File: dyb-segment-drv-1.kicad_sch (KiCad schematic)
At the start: 8 parts, among them U1 AP2112K-1.8, U2 SN74AUP2G08, U3 74AUC2G32, U4 Inverter_Schmitt_Dual

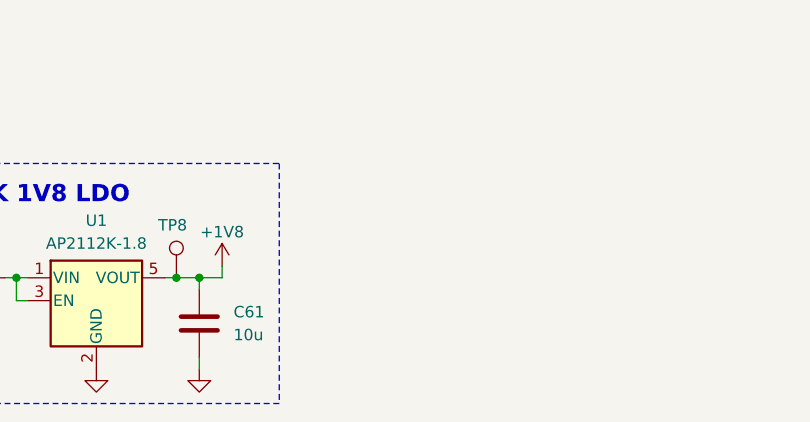
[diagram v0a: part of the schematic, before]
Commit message: schem: add cr2032 holder
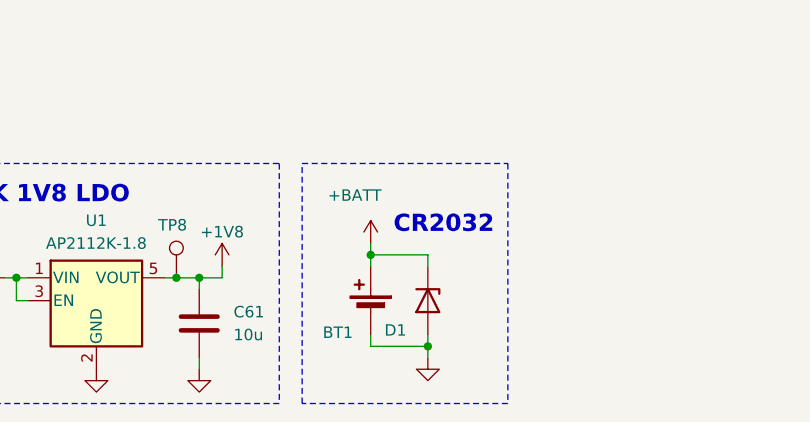
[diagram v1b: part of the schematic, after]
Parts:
- added BT1: Battery_Cell, GLCS:BatteryHolder_MYOUNG_BS-08-B2AA016, symbol Device:Battery_Cell
- added D1: H5VU10U, GLCS:Diode_DFN1006, symbol GLCS:H5VU10U
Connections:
- net +BATT: now also BT1.1 (+), D1.1 (K)
- net GND: now also BT1.2 (-), D1.2 (A)
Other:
- note added: "CR2032"

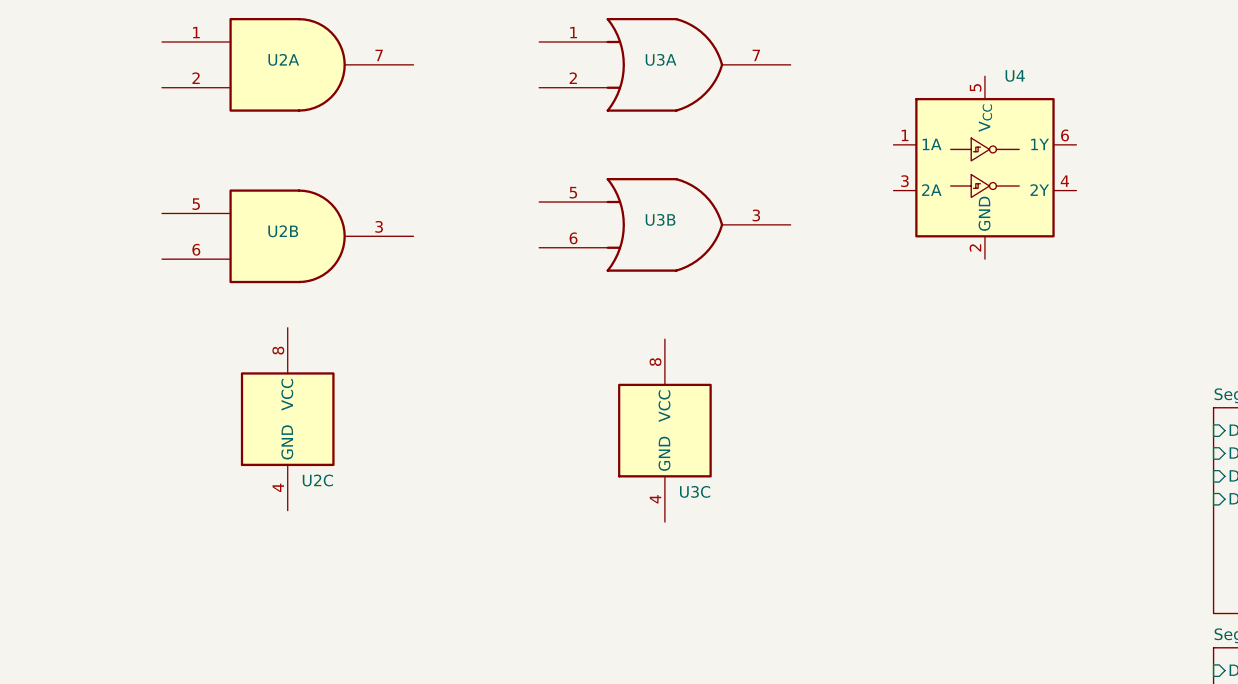
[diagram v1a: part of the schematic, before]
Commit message: schem: remove extra gates
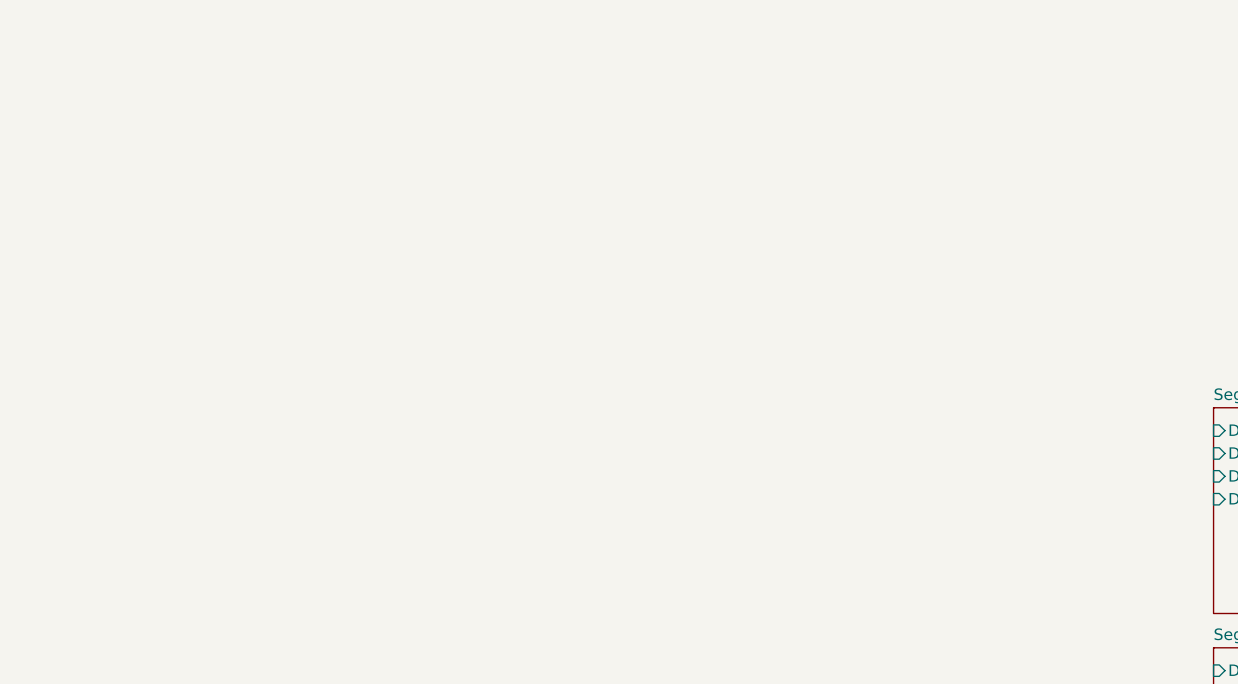
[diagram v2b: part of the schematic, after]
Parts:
- removed U2: SN74AUP2G08, Package_SO:VSSOP-8_2.3x2mm_P0.5mm, symbol GLCS:SN74AUP2G08
- removed U3: 74AUC2G32, Package_DFN_QFN:QFN-20-1EP_5x5mm_P0.65mm_EP3.35x3.35mm, symbol 74xGxx:74AUC2G32
- removed U4: Inverter_Schmitt_Dual, Package_TO_SOT_SMD:SOT-23-6, symbol 74xGxx:Inverter_Schmitt_Dual

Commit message: schem: add b2b connector
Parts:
- added J1: Conn_01x10, symbol Connector_Generic:Conn_01x10
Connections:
- net GND: now also J1.10 (Pin_10)
- new net A0: J1.1 (Pin_1)
- new net A1: J1.2 (Pin_2)
- new net A2: J1.3 (Pin_3)
- new net A3: J1.4 (Pin_4)
- new net B0: J1.5 (Pin_5)
- new net B1: J1.6 (Pin_6)
- new net B2: J1.7 (Pin_7)
- new net B3: J1.8 (Pin_8)
- no-connect marks 0 -> 1

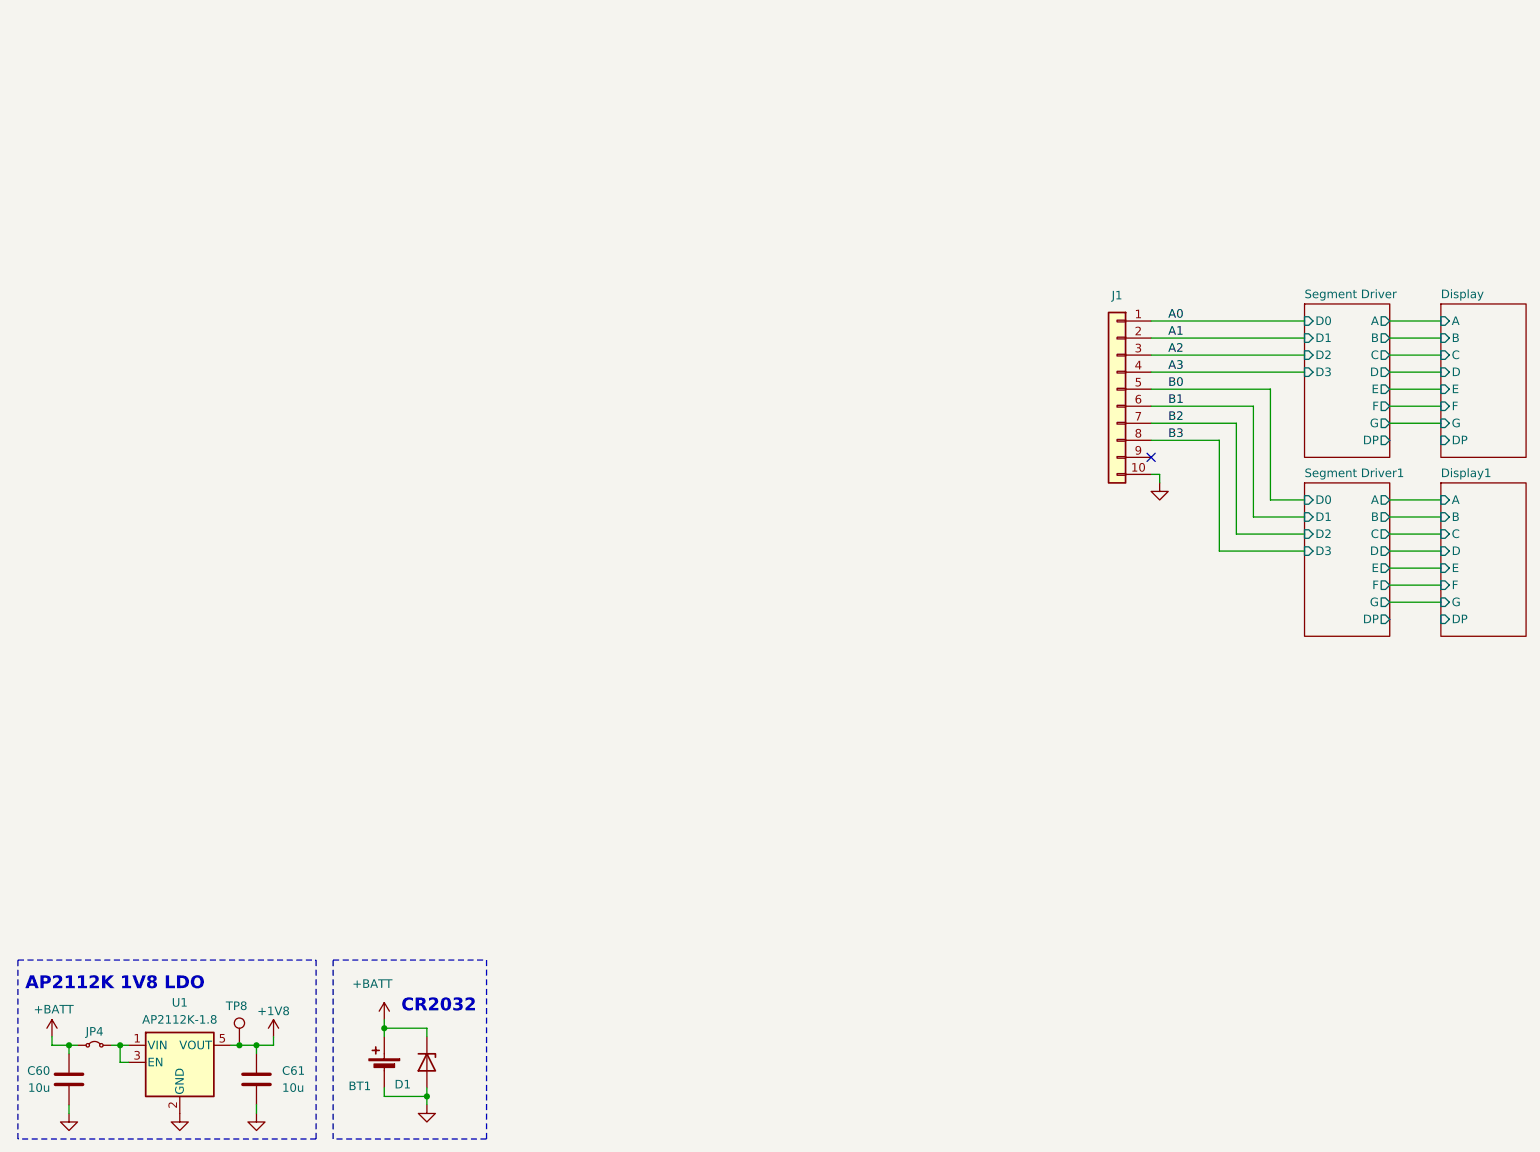
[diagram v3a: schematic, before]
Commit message: schem: add batt switch
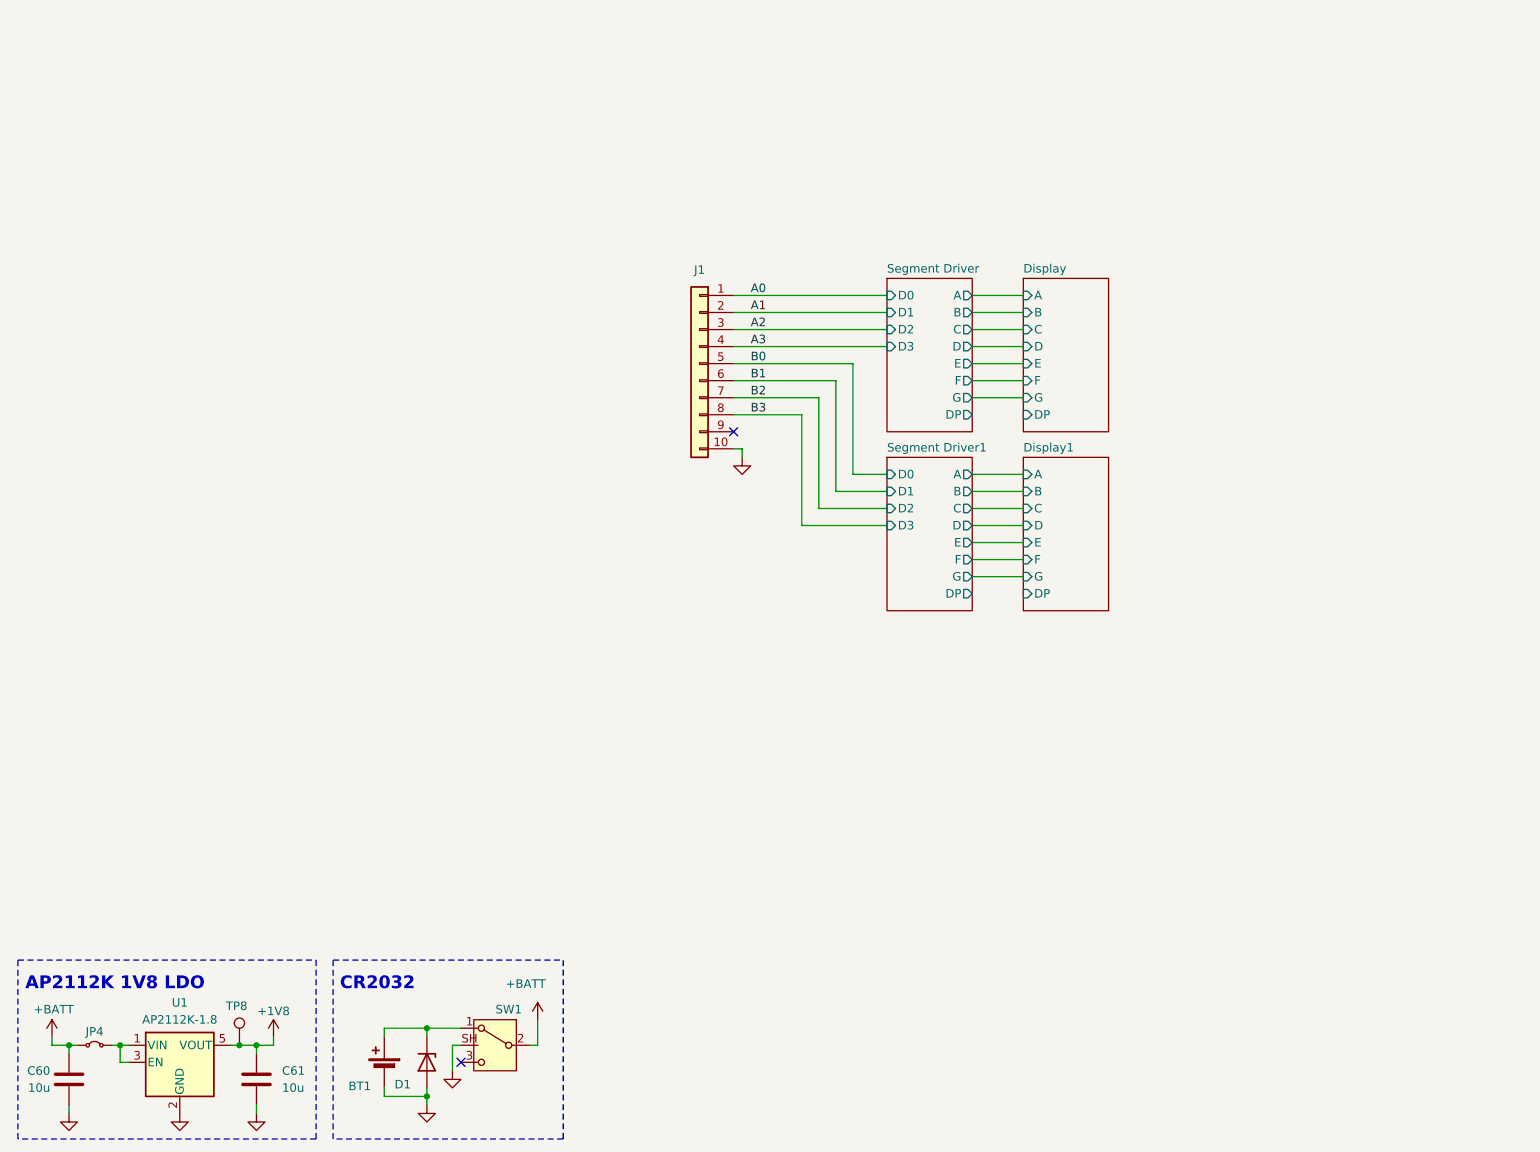
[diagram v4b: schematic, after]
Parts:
- added SW1: SW_SPDT, Button_Switch_SMD:SW_SPDT_Shouhan_MSK12C02, symbol Switch:SW_SPDT
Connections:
- net +BATT: now also SW1.2 (B); no longer BT1.1 (+), D1.1 (K)
- net GND: now also SW1.SH
- new net: BT1.1 (+), D1.1 (K), SW1.1 (A)
- no-connect marks 1 -> 2
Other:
- moved on the sheet: J1

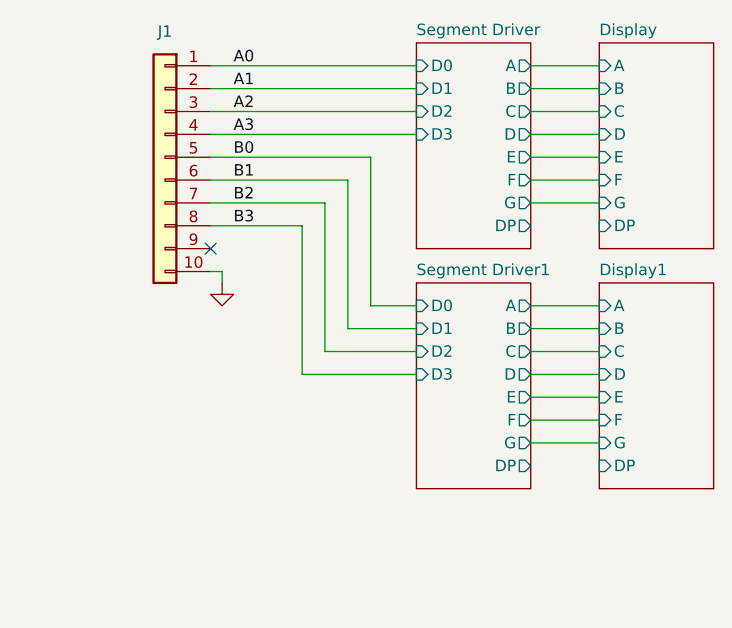
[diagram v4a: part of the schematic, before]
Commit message: schem: add test points
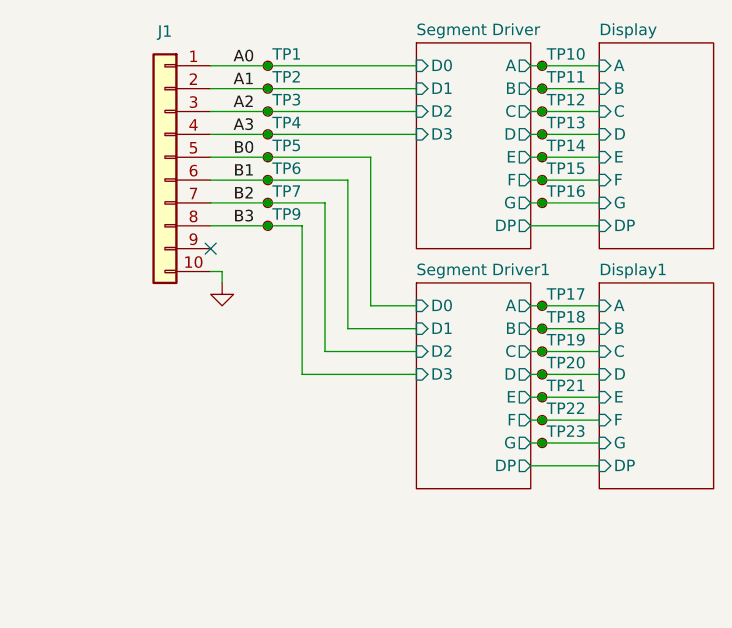
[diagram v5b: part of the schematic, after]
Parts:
- added TP1, TP10, TP11, TP12, TP13, TP14, TP15, TP16, TP17, TP18, TP19, TP2, TP20, TP21, TP22, TP23, TP3, TP4, TP5, TP6, TP7, TP9: TestPoint_Small, symbol Connector:TestPoint_Small
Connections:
- net A0: now also TP1.1
- net A1: now also TP2.1
- net A2: now also TP3.1
- net A3: now also TP4.1
- net B0: now also TP5.1
- net B1: now also TP6.1
- net B2: now also TP7.1
- net B3: now also TP9.1
- net Display/A: now also TP10.1
- net Display/B: now also TP11.1
- net Display/C: now also TP12.1
- net Display/D: now also TP13.1
- net Display/E: now also TP14.1
- net Display/F: now also TP15.1
- net Display/G: now also TP16.1
- net Display1/A: now also TP17.1
- net Display1/B: now also TP18.1
- net Display1/C: now also TP19.1
- net Display1/D: now also TP20.1
- net Display1/E: now also TP21.1
- net Display1/F: now also TP22.1
- net Display1/G: now also TP23.1

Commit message: schem: run and fix ERC
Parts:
- added TP26, TP27: TestPoint_Small, symbol Connector:TestPoint_Small
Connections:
- net Display/DP: now also TP27.1
- net Display1/DP: now also TP26.1
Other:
- sheet Segment Driver ports: added none; removed DP
- sheet Segment Driver1 ports: added none; removed DP

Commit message: schem: add missing footprints
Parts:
- J1: footprint (none) -> GLCS:KYOCERA_AVX9159-006
- TP1, TP10, TP11, TP12, TP13, TP14, TP15, TP16, TP17, TP18, TP19, TP2, TP20, TP21, TP22, TP23, TP26, TP27, TP3, TP4, TP5, TP6, TP7, TP9: footprint (none) -> TestPoint:TestPoint_Pad_D1.0mm
- TP8: footprint TestPoint:TestPoint_Pad_D2.0mm -> TestPoint:TestPoint_Pad_D1.0mm
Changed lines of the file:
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@@
 			)
 		)
-		(property "Footprint" ""
+		(property "Footprint" "TestPoint:TestPoint_Pad_D1.0mm"
 			(at 133.35 77.47 0)
 			(hide yes)
@@
 			)
 		)
-		(property "Footprint" ""
+		(property "Footprint" "TestPoint:TestPoint_Pad_D1.0mm"
 			(at 163.83 77.47 0)
 			(hide yes)
@@
 			)
 		)
-		(property "Footprint" ""
+		(property "Footprint" "GLCS:KYOCERA_AVX9159-006"
 			(at 116.84 80.01 0)
 			(hide yes)
@@
 			)
 		)
-		(property "Footprint" ""
+		(property "Footprint" "TestPoint:TestPoint_Pad_D1.0mm"
 			(at 133.35 82.55 0)
 			(hide yes)
@@
 			)
 		)
-		(property "Footprint" "TestPoint:TestPoint_Pad_D2.0mm"
+		(property "Footprint" "TestPoint:TestPoint_Pad_D1.0mm"
 			(at 53.34 181.61 0)
 			(hide yes)
@@
 			)
 		)
-		(property "Footprint" ""
+		(property "Footprint" "TestPoint:TestPoint_Pad_D1.0mm"
 			(at 163.83 111.76 0)
 			(hide yes)
@@
 			)
 		)
-		(property "Footprint" ""
+		(property "Footprint" "TestPoint:TestPoint_Pad_D1.0mm"
 			(at 163.83 114.3 0)
 			(hide yes)
@@
 			)
 		)
-		(property "Footprint" ""
+		(property "Footprint" "TestPoint:TestPoint_Pad_D1.0mm"
 			(at 133.35 85.09 0)
 			(hide yes)
@@
 			)
 		)
-		(property "Footprint" ""
+		(property "Footprint" "TestPoint:TestPoint_Pad_D1.0mm"
 			(at 163.83 74.93 0)
 			(hide yes)
@@
 			)
 		)
-		(property "Footprint" ""
+		(property "Footprint" "TestPoint:TestPoint_Pad_D1.0mm"
 			(at 163.83 80.01 0)
 			(hide yes)
@@
 			)
 		)
-		(property "Footprint" ""
+		(property "Footprint" "TestPoint:TestPoint_Pad_D1.0mm"
 			(at 163.83 104.14 0)
 			(hide yes)
@@
 			)
 		)
-		(property "Footprint" ""
+		(property "Footprint" "TestPoint:TestPoint_Pad_D1.0mm"
 			(at 163.83 85.09 0)
 			(hide yes)
@@
 			)
 		)
-		(property "Footprint" ""
+		(property "Footprint" "TestPoint:TestPoint_Pad_D1.0mm"
 			(at 163.83 109.22 0)
 			(hide yes)
@@
 			)
 		)
-		(property "Footprint" ""
+		(property "Footprint" "TestPoint:TestPoint_Pad_D1.0mm"
 			(at 163.83 87.63 0)
 			(hide yes)
@@
 			)
 		)
-		(property "Footprint" ""
+		(property "Footprint" "TestPoint:TestPoint_Pad_D1.0mm"
 			(at 133.35 87.63 0)
 			(hide yes)
@@
 			)
 		)
-		(property "Footprint" ""
+		(property "Footprint" "TestPoint:TestPoint_Pad_D1.0mm"
 			(at 163.83 69.85 0)
 			(hide yes)
@@
 			)
 		)
-		(property "Footprint" ""
+		(property "Footprint" "TestPoint:TestPoint_Pad_D1.0mm"
 			(at 133.35 72.39 0)
 			(hide yes)
@@
 			)
 		)
-		(property "Footprint" ""
+		(property "Footprint" "TestPoint:TestPoint_Pad_D1.0mm"
 			(at 163.83 99.06 0)
 			(hide yes)
@@
 			)
 		)
-		(property "Footprint" ""
+		(property "Footprint" "TestPoint:TestPoint_Pad_D1.0mm"
 			(at 163.83 72.39 0)
 			(hide yes)
@@
 			)
 		)
-		(property "Footprint" ""
+		(property "Footprint" "TestPoint:TestPoint_Pad_D1.0mm"
 			(at 163.83 96.52 0)
 			(hide yes)
@@
 			)
 		)
-		(property "Footprint" ""
+		(property "Footprint" "TestPoint:TestPoint_Pad_D1.0mm"
 			(at 133.35 74.93 0)
 			(hide yes)
@@
 			)
 		)
-		(property "Footprint" ""
+		(property "Footprint" "TestPoint:TestPoint_Pad_D1.0mm"
 			(at 133.35 80.01 0)
 			(hide yes)
@@
 			)
 		)
-		(property "Footprint" ""
+		(property "Footprint" "TestPoint:TestPoint_Pad_D1.0mm"
 			(at 163.83 106.68 0)
 			(hide yes)
@@
 			)
 		)
-		(property "Footprint" ""
+		(property "Footprint" "TestPoint:TestPoint_Pad_D1.0mm"
 			(at 133.35 69.85 0)
 			(hide yes)
@@
 			)
 		)
-		(property "Footprint" ""
+		(property "Footprint" "TestPoint:TestPoint_Pad_D1.0mm"
 			(at 163.83 82.55 0)
 			(hide yes)
@@
 			)
 		)
-		(property "Footprint" ""
+		(property "Footprint" "TestPoint:TestPoint_Pad_D1.0mm"
 			(at 163.83 101.6 0)
 			(hide yes)
